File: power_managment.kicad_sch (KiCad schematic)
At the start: 18 parts, among them J2 RAPC722X, U3 LM2576HVS-5, U4 LM2576HVS-5, U5 AMS1117-3.3

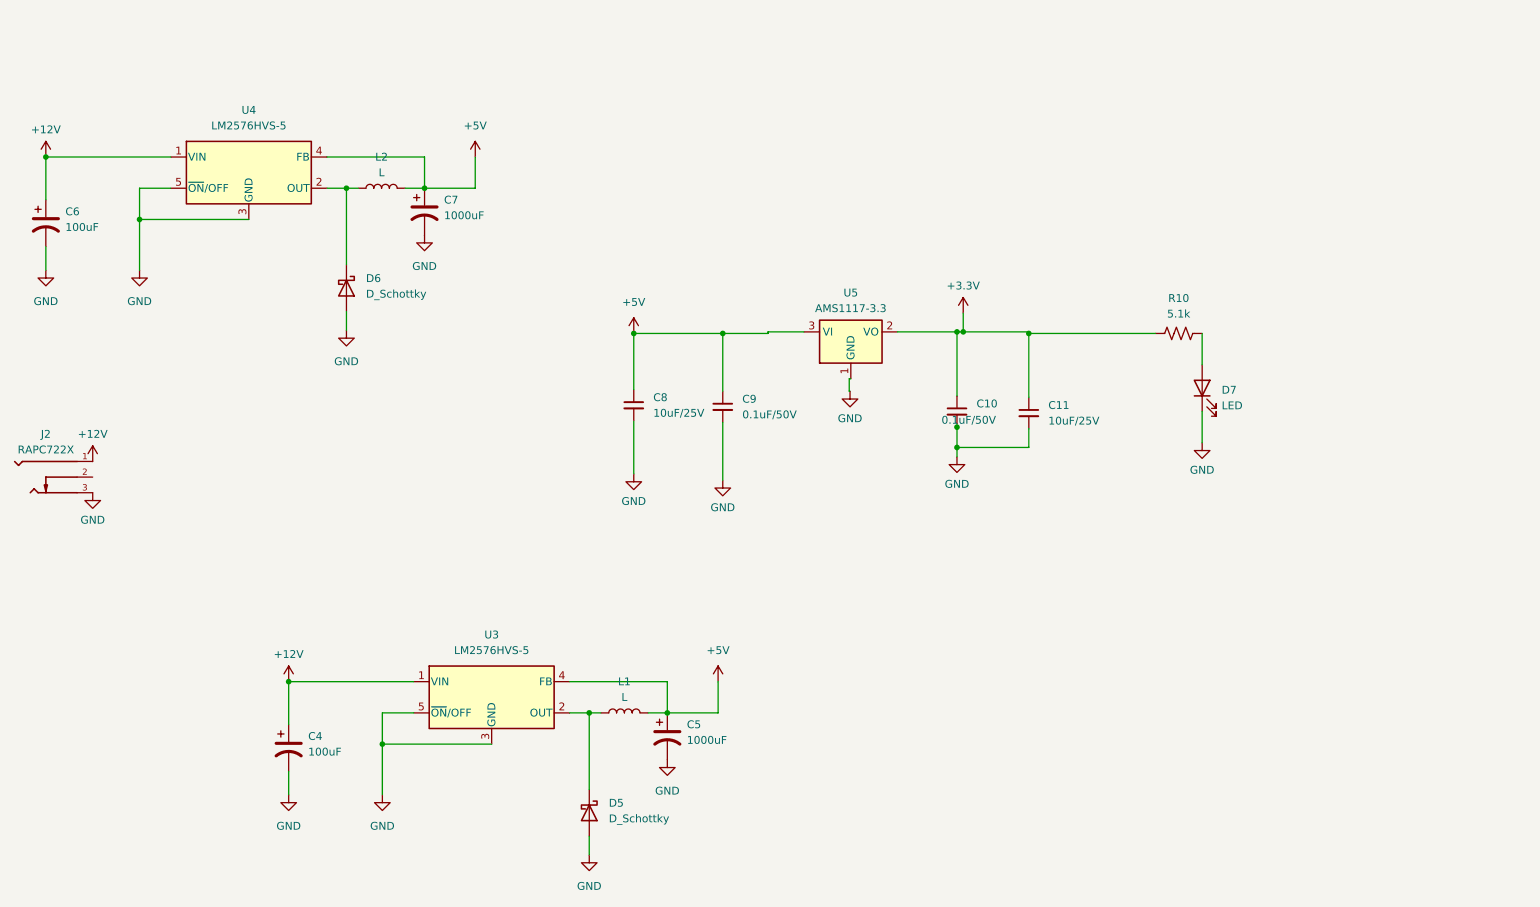
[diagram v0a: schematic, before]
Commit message: Base changes
Deleted the redundant files.
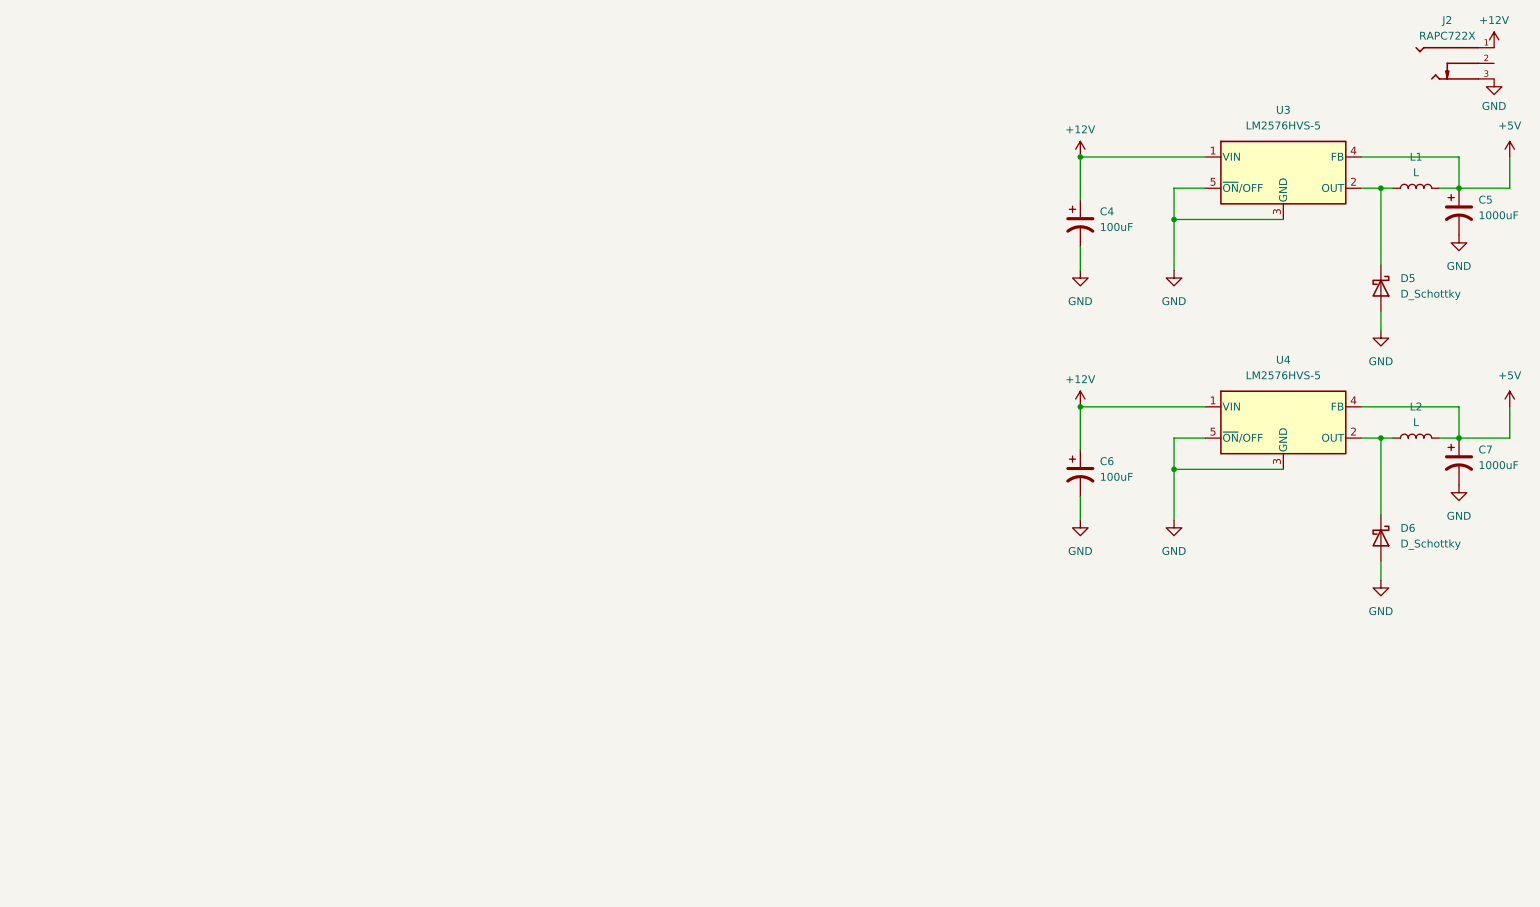
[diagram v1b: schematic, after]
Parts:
- removed C10, C9: 0.1uF/50V, symbol Device:C_Small
- removed C11, C8: 10uF/25V, symbol Device:C_Small
- removed D7: LED, symbol Device:LED
- removed R10: 5.1k, symbol Device:R_US
- removed U5: AMS1117-3.3, Package_TO_SOT_SMD:SOT-223-3_TabPin2, symbol Regulator_Linear:AMS1117-3.3
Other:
- moved on the sheet: C4, C5, C6, C7, D5, D6, J2, L1, L2, U3, U4
